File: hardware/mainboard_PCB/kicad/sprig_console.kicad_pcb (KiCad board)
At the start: 2 copper layers, 139.7 x 64.8 mm, 42 parts, among them J1 1020_battery_holder, J2 Conn_PinHeader_2x03_P2.54mm_V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, SW1 W, SW2 A, SW3 S, SW4 D, SW5 I, SW6 J, SW7 K, SW8 L, SW9 Slideswitch, U2 MAX98357AETE+, U5 Pico

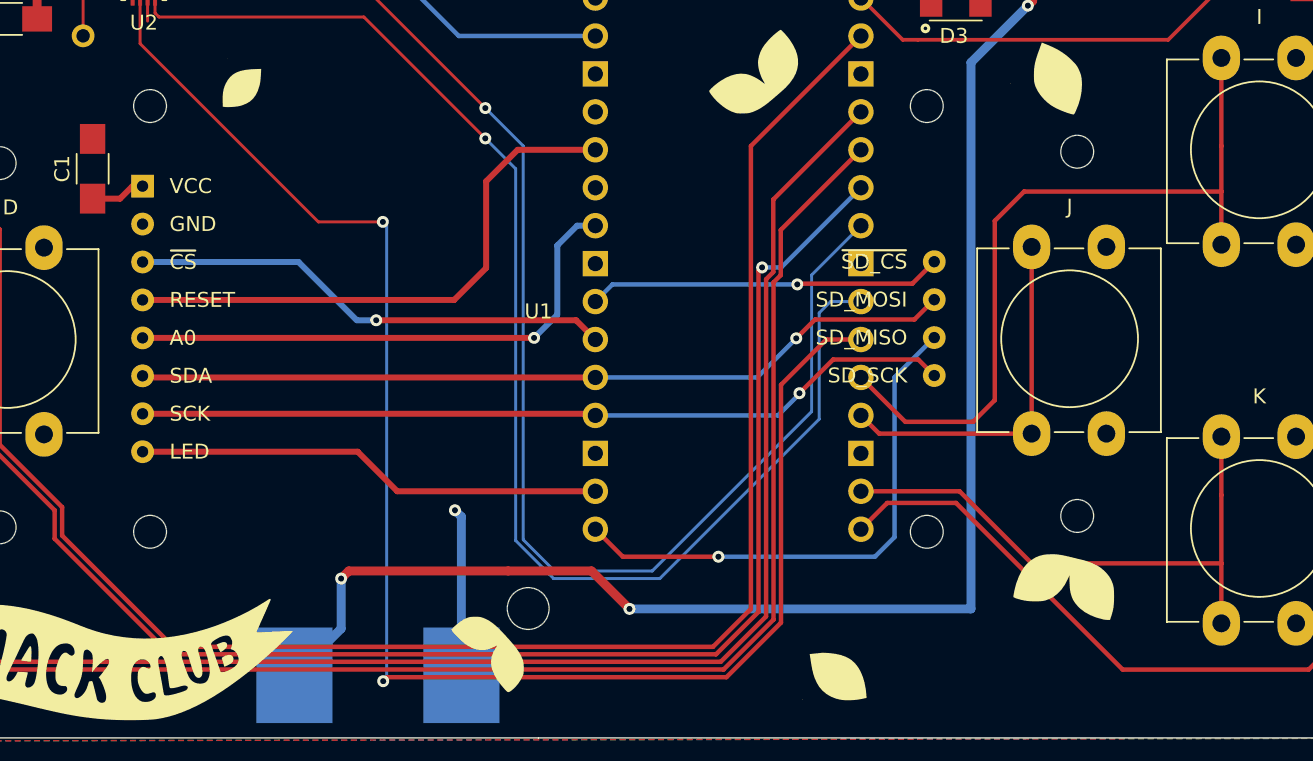
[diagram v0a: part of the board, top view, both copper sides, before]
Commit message: temp under screen headers
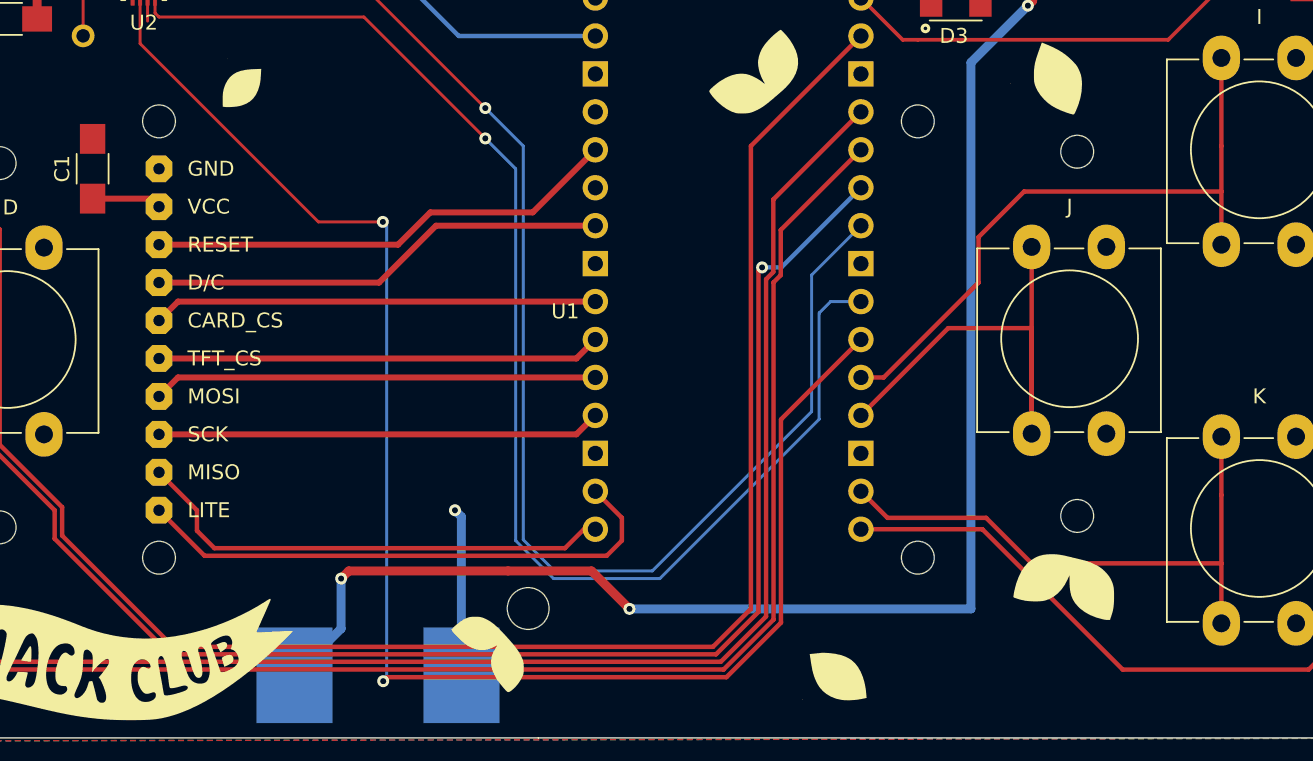
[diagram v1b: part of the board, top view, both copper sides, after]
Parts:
- U1: value ~ -> Adafruit_TFT_ST7735; footprint sprig:TFT_MSP1803 -> fab:TFT_ST7735
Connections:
- U1 pad 1: +3V3 -> LITE
- U1 pad 10: MOSI -> GND
- U1 pad 2: GND -> MISO
- U1 pad 3: TFT_CS -> SCK
- U1 pad 4: RESET -> MOSI
- U1 pad 5: D/C -> TFT_CS
- U1 pad 6: MOSI -> CARD_CS
- U1 pad 7: SCK -> D/C
- U1 pad 8: LITE -> RESET
- U1 pad 9: CARD_CS -> +3V3
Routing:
- net MOSI: track 55.6 -> 29.7 mm, vias 1 -> 0
- net SCK: track 55.3 -> 29.7 mm, vias 1 -> 0
- net BTN_J: track 24.4 -> 33.4 mm
- net BTN_I: track 51.9 -> 43.6 mm
- net RESET: track 38.6 -> 32.3 mm
- net D/C: track 36.7 -> 30.8 mm, vias 1 -> 0
- net CARD_CS: track 23.8 -> 29.7 mm, vias 1 -> 0
- net LITE: track 31.4 -> 36.7 mm
- net MISO: track 35.8 -> 32.6 mm, vias 1 -> 0
- net TFT_CS: track 32.5 -> 29.7 mm, vias 1 -> 0
- net BTN_L: track 66.4 -> 65.0 mm
- net LRCLK: track 106.1 -> 104.8 mm
- net +3V3: track 15.9 -> 16.9 mm

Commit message: new board for new screen (#2430)
* new board design w/ cheaper screens

* new board design w/ cheaper screens

* add nora as co author

Co-authored-by: Nora <nora@hackclub.com>

* try again

wahoo



Co-authored-by: Nora <nora@hackclub.com>

* Update fp-lib-table


Co-authored-by: 24c02 <163450896+24c02@users.noreply.github.com>

---------

Co-authored-by: Nora <nora@hackclub.com>
Co-authored-by: 24c02 <163450896+24c02@users.noreply.github.com>
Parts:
- U1: value Adafruit_TFT_ST7735 -> ~; footprint fab:TFT_ST7735 -> sprig:TFT_MSP1803
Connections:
- U1 pad 1: LITE -> +3V3
- U1 pad 10: GND -> MOSI
- U1 pad 2: MISO -> GND
- U1 pad 3: SCK -> TFT_CS
- U1 pad 4: MOSI -> RESET
- U1 pad 5: TFT_CS -> D/C
- U1 pad 6: CARD_CS -> MOSI
- U1 pad 7: D/C -> SCK
- U1 pad 8: RESET -> LITE
- U1 pad 9: +3V3 -> CARD_CS
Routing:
- net MOSI: track 29.7 -> 55.6 mm, vias 0 -> 1
- net SCK: track 29.7 -> 55.3 mm, vias 0 -> 1
- net BTN_J: track 33.4 -> 24.4 mm
- net BTN_I: track 43.6 -> 51.9 mm
- net RESET: track 32.3 -> 38.6 mm
- net D/C: track 30.8 -> 36.7 mm, vias 0 -> 1
- net CARD_CS: track 29.7 -> 23.8 mm, vias 0 -> 1
- net LITE: track 36.7 -> 31.4 mm
- net MISO: track 32.6 -> 35.8 mm, vias 0 -> 1
- net TFT_CS: track 29.7 -> 32.5 mm, vias 0 -> 1
- net BTN_L: track 65.0 -> 66.4 mm
- net LRCLK: track 104.8 -> 106.1 mm
- net +3V3: track 16.9 -> 15.9 mm
